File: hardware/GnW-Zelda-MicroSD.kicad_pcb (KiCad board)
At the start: 2 copper layers, 28.4 x 29.7 mm, 11 parts, among them J1 Castellated_Edge_7P, J2 MicroSD_Socket, J3 VBAT_Tab, U1 RT9193-28GB

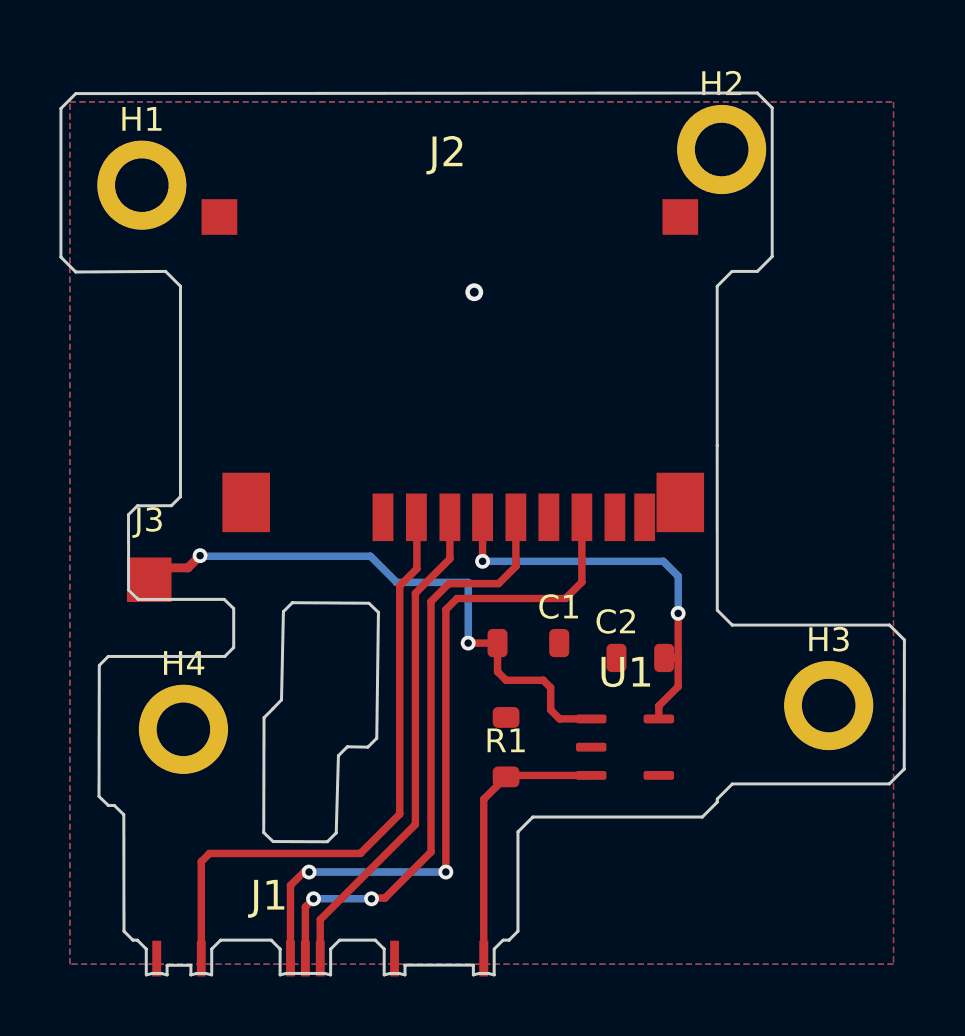
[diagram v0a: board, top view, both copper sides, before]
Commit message: Swap J2/J3/U1 to PrimoAngelo's real footprints, fix ref-designator and net-naming bugs
J2 (microSD socket) and J3 (VBAT tab) now use real MSD1A/Pad_1x1_5
geometry from PrimoAngelo's native KiCad library instead of RE'd
approximations; U1 gets a real RT9193 STEP model. C1/C2/R1 get a second,
real hand-solder-0805 footprint stacked at their original location for
package-size flexibility.

Also fixes: schematic/PCB reference-designator swap (J2/J3, U1/U2), a
batch of inconsistent net names left over from re-syncing the PCB from
schematic (local net labels converted to global to prevent recurrence),
and 8 undersized vias failing min-hole-size DRC.
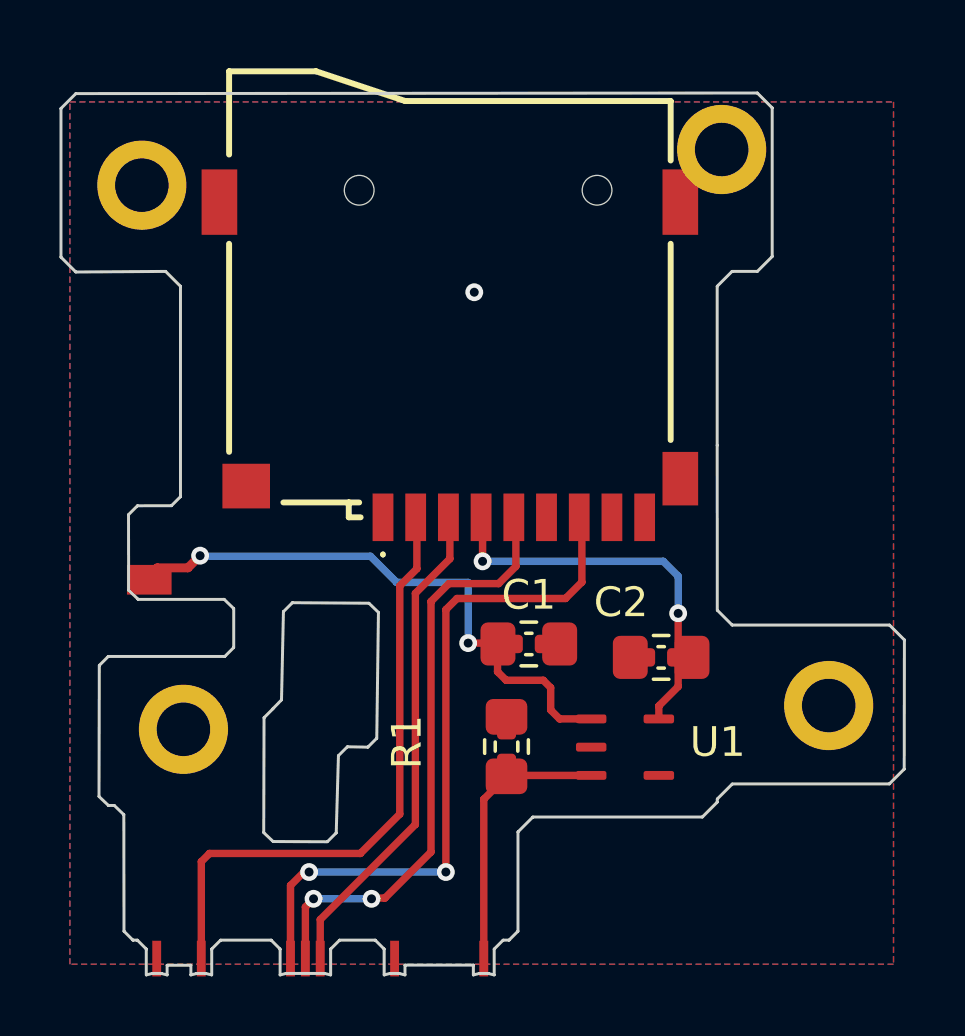
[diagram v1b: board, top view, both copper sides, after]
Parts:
- added REF**: R_0805_2012Metric_Pad1.20x1.40mm_HandSolder, Resistor_SMD:R_0805_2012Metric_Pad1.20x1.40mm_HandSolder, F.Cu at (150.8, 57.1)
- added REF**: C_0805_2012Metric_Pad1.18x1.45mm_HandSolder, Capacitor_SMD:C_0805_2012Metric_Pad1.18x1.45mm_HandSolder, F.Cu at (151.6, 53.7)
- added REF**: C_0805_2012Metric_Pad1.18x1.45mm_HandSolder, Capacitor_SMD:C_0805_2012Metric_Pad1.18x1.45mm_HandSolder, F.Cu at (156.0, 54.1)
- C1: footprint Passive_exact_C1 -> Capacitor_SMD:C_0402_1005Metric
- C2: footprint Passive_exact_C2 -> Capacitor_SMD:C_0402_1005Metric
- J2: value MicroSD_Socket -> MicroSD_Socket_TFP09; footprint MicroSD_Socket_J9 -> PrimoAngelo_FG_MicroSD:MSD1A
- J3: value VBAT_Tab -> Battery_Tap_2P; footprint Castellated_VBAT_Tab -> PrimoAngelo_Pad:Pad_1x1_5
- R1: footprint Passive_exact_R1 -> Resistor_SMD:R_0402_1005Metric
- moved C2 165.1 mm to (156.0, 54.1), turned to 180 degrees
- moved R1 161.3 mm to (150.8, 57.1), turned to 90 degrees
- moved C1 160.8 mm to (151.6, 53.7)
- moved J2 154.8 mm to (148.9, 42.3), turned to 180 degrees
- moved J3 148.0 mm to (138.8, 51.5), turned to 90 degrees
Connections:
- net EN_LDO renamed EN_PA15
- C1 pad 1: GND -> VBAT_4V2
- C1 pad 2: VBAT_4V2 -> GND
- C2 pad 1: GND -> VDD_SD_2V8
- C2 pad 2: VDD_SD_2V8 -> GND
- J1 pad 6: (no net) -> unconnected-(J1-NC-Pad6)
- J2 pad 1: (no net) -> unconnected-(J2-DAT2-Pad1)
- J2 pad 11: GND -> (no net)
- J2 pad 8: (no net) -> unconnected-(J2-DAT1-Pad8)
- J2 pad 9: (no net) -> unconnected-(J2-CD-Pad9)
- U1 pad 4: (no net) -> unconnected-(U1-BYP-Pad4)

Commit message: Clean up schematic layout and silkscreen
Manual schematic relayout (wires/symbols, no connectivity changes --
component roster and net topology unchanged, verified via ERC/DRC). PCB
silkscreen cleanup: R1/C1/C2 values moved from F.Fab to F.SilkS so
they're visible on the physical board, U1's reference text replaced with
its part number (RT9193-28GB) since it's the board's only IC and "U1"
isn't descriptive, and a "4V" label added near the VBAT tap (J3).
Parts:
- renumbered U1 to RT9193-28GB
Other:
- board text added: "4V"
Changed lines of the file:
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@@
 		(at 0 0)
 		(descr "RT9193-28GB LDO -- exact pad positions/sizes (aperture D20, 1.025x0.3mm) replicated from source")
-		(property "Reference" "U1"
-			(at 157.9 57 0)
-			(layer "F.SilkS")
-			(effects
-				(font
-					(size 1 1)
-					(thickness 0.15)
+		(property "Reference" "RT9193-28GB"
+			(at 154.75 58.9 0)
+			(layer "F.SilkS")
+			(effects
+				(font
+					(size 0.5 0.5)
+					(thickness 0.125)
 				)
 			)
@@
 		(property "Value" "100k"
 			(at 0.1 -1.65 90)
-			(layer "F.Fab")
+			(layer "F.SilkS")
 			(effects
 				(font
@@
 		(tags "capacitor")
 		(property "Reference" "C2"
-			(at 1.35 1.85 0)
+			(at 0 1.7 0)
 			(layer "F.SilkS")
 			(effects
@@
 		(property "Value" "1uF"
 			(at -3.1 0.3 0)
-			(layer "F.Fab")
+			(layer "F.SilkS")
 			(effects
 				(font
@@
 		(property "Value" "1uF"
 			(at -3.6 -0.1 0)
-			(layer "F.Fab")
+			(layer "F.SilkS")
 			(effects
 				(font
@@
 		(layer "Edge.Cuts")
 	)
+	(gr_text "4V"
+		(at 138.2 50.7 0)
+		(layer "F.SilkS")
+		(effects
+			(font
+				(size 1 1)
+				(thickness 0.1)
+			)
+			(justify left bottom)
+		)
+	)
 	(via
